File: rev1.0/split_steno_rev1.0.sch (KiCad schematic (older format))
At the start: 82 parts, among them J0 Audio-Jack-4, J1 Audio-Jack-3, K0 KEYSW, K1 KEYSW, K10 KEYSW, K11 KEYSW, K12 KEYSW, K13 KEYSW, K14 KEYSW, K15 KEYSW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

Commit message: added ws2812b
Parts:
- removed J1: Audio-Jack-3, symbol Audio-Jack-3
- removed R16: R, symbol R
- added LED0, LED1, LED2, LED3, LED4: WS2812B, symbol WS2812B
- added Q0: BC547, TO_SOT_Packages_THT:TO-92_Molded_Narrow, symbol BC547
- added R19, R20, R?: R, symbol R
- renumbered R17 to R16, R19 to R17, U1 to U0
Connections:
- net labels added: data0, data1, pwm0, rgb0
- net labels removed: i2c, serial, ws2812b
- wire segments 189 -> 243
- no-connect marks 5 -> 6
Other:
- moved on the sheet: D0, D1, D10, D11, D12, D13, D14, D15, D16, D17, D18, D19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

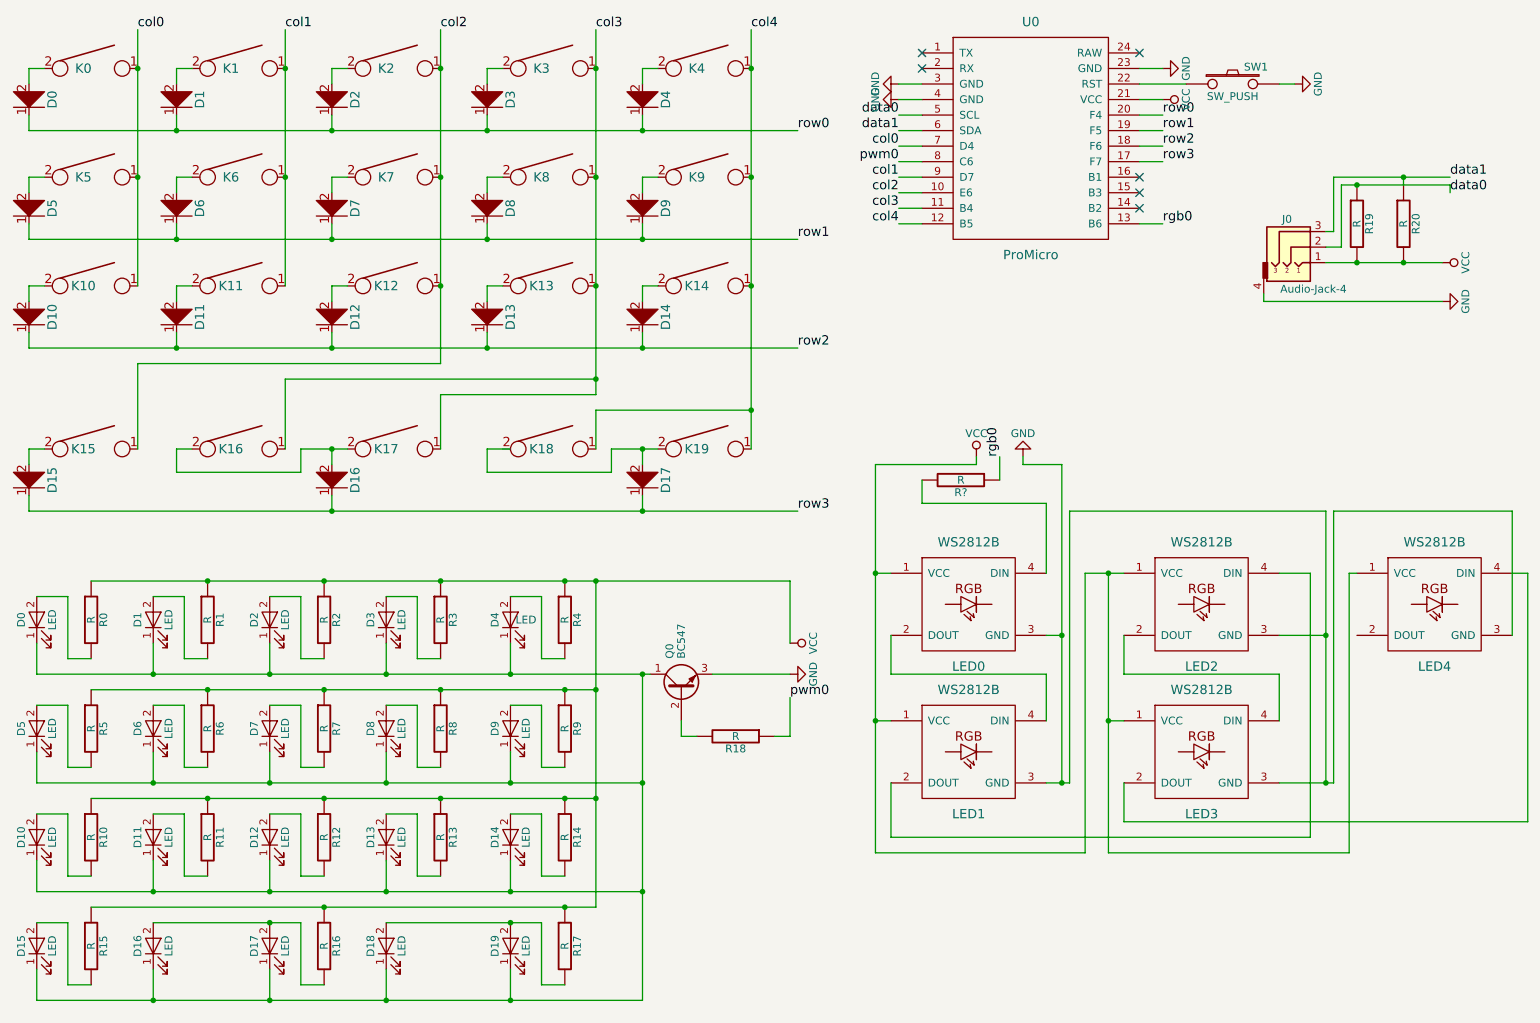
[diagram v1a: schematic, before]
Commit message: cleaned up schematic
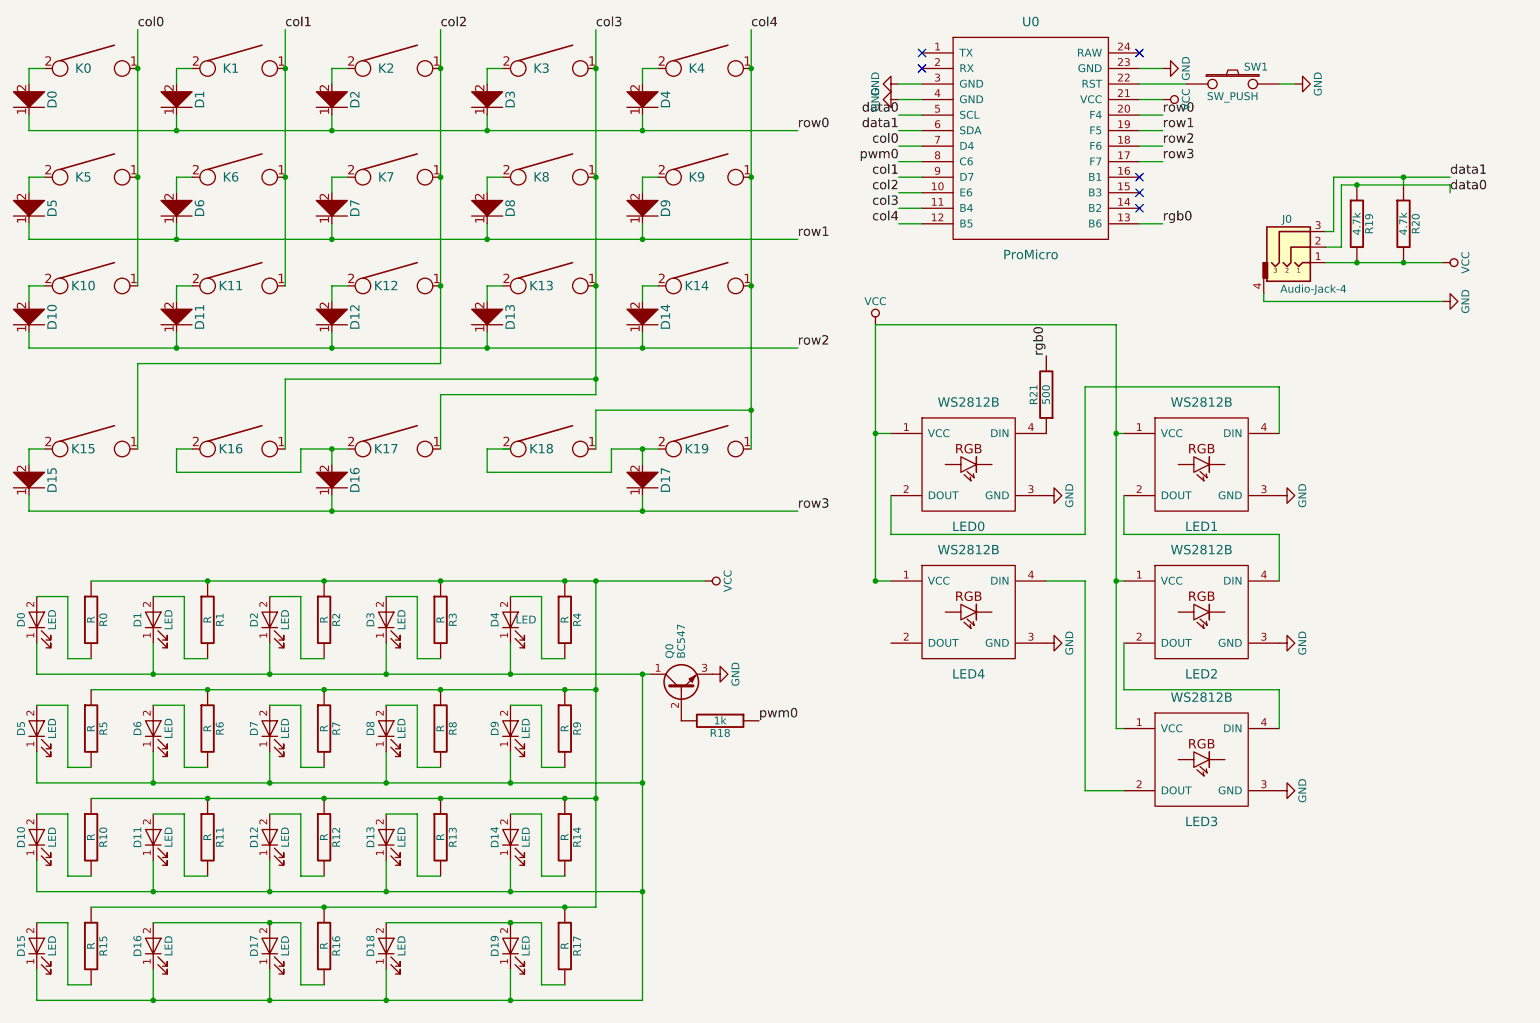
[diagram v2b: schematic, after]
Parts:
- R18: value R -> 1k
- R19, R20: value R -> 4.7k
- R21: renamed from R?; value R -> 500
- renumbered LED2 to LED1, LED3 to LED2, LED4 to LED3, LED1 to LED4
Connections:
- net rgb0: now also R21.2; no longer R21.1
- net at LED0.2 (DOUT): now also LED1.4 (DIN); no longer LED4.4 (DIN)
- net at LED0.4 (DIN): now also R21.1; no longer R21.2
- net at LED4.2 (DOUT): no longer LED1.4 (DIN)
- net at LED3.2 (DOUT): now also LED4.4 (DIN)
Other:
- moved on the sheet: LED0, LED1, LED2, LED3, LED4, R18, R21

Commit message: removed LED backlighting
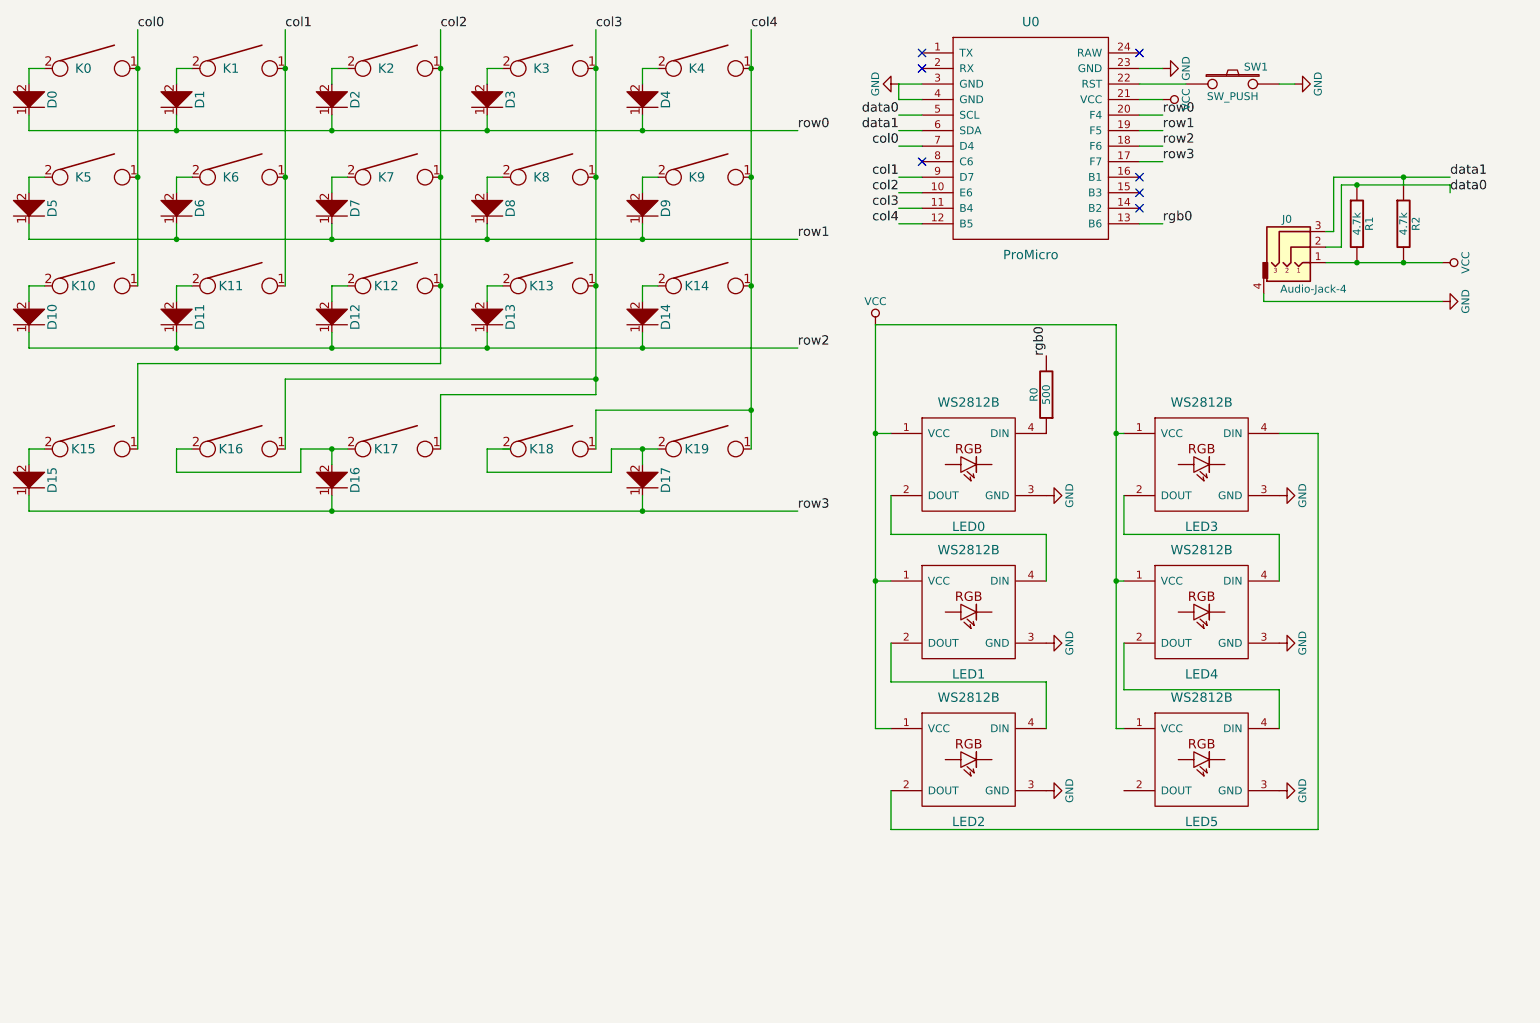
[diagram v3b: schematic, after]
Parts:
- removed D0, D1, D10, D11, D12, D13, D14, D15, D16, D17, D18, D19, D2, D3, D4, D5, D6, D7, D8, D9: LED, symbol LED
- removed Q0: BC547, TO_SOT_Packages_THT:TO-92_Molded_Narrow, symbol BC547
- removed R0, R1, R10, R11, R12, R13, R14, R15, R16, R17, R2, R3, R4, R5, R6, R7, R8, R9: R, symbol R
- removed R18: 1k, symbol R
- added LED2: WS2812B, WS2812B:WS2812B, symbol WS2812B
- D0, D1, D10, D11, D12, D13, D14, D15, D16, D17, D2, D3, D4, D5, D6, D7, D8, D9: footprint (none) -> Keebio-Parts:Diode-dual
- J0: footprint (none) -> Keebio-Parts:TRRS-PJ-320A-dual
- K0, K1, K10, K11, K12, K13, K14, K15, K17, K19, K2, K3, K4, K5, K6, K7, K8, K9: footprint (none) -> Keebio-Parts:Hybrid_PCB_100H_Dual_hole
- K16, K18: footprint (none) -> Keebio-Parts:Hybrid_PCB_200H-dual
- LED0: footprint (none) -> WS2812B:WS2812B
- LED1: renamed from LED4; footprint (none) -> WS2812B:WS2812B
- LED3: renamed from LED1; footprint (none) -> WS2812B:WS2812B
- LED4: renamed from LED2; footprint (none) -> WS2812B:WS2812B
- LED5: renamed from LED3; footprint (none) -> WS2812B:WS2812B
- R0: renamed from R21; footprint (none) -> Keebio-Parts:Resistor-Hybrid
- R1: renamed from R19; footprint (none) -> Keebio-Parts:Resistor-Hybrid
- R2: renamed from R20; footprint (none) -> Keebio-Parts:Resistor-Hybrid
- SW1: footprint (none) -> Keebio-Parts:SW_Tactile_SPST_Angled_MJTP1117
- U0: footprint (none) -> Keebio-Parts:ArduinoProMicro
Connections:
- net GND: now also LED2.3 (GND)
- net VCC: now also LED2.1 (VCC)
- net at LED0.2 (DOUT): now also LED1.4 (DIN); no longer LED3.4 (DIN)
- net at LED1.2 (DOUT): now also LED2.4 (DIN)
- net at LED5.2 (DOUT): no longer LED1.4 (DIN)
- net pwm0: no longer names the net of U0.8 (C6)
- new net: LED2.2 (DOUT), LED3.4 (DIN)
- no-connect marks 6 -> 7

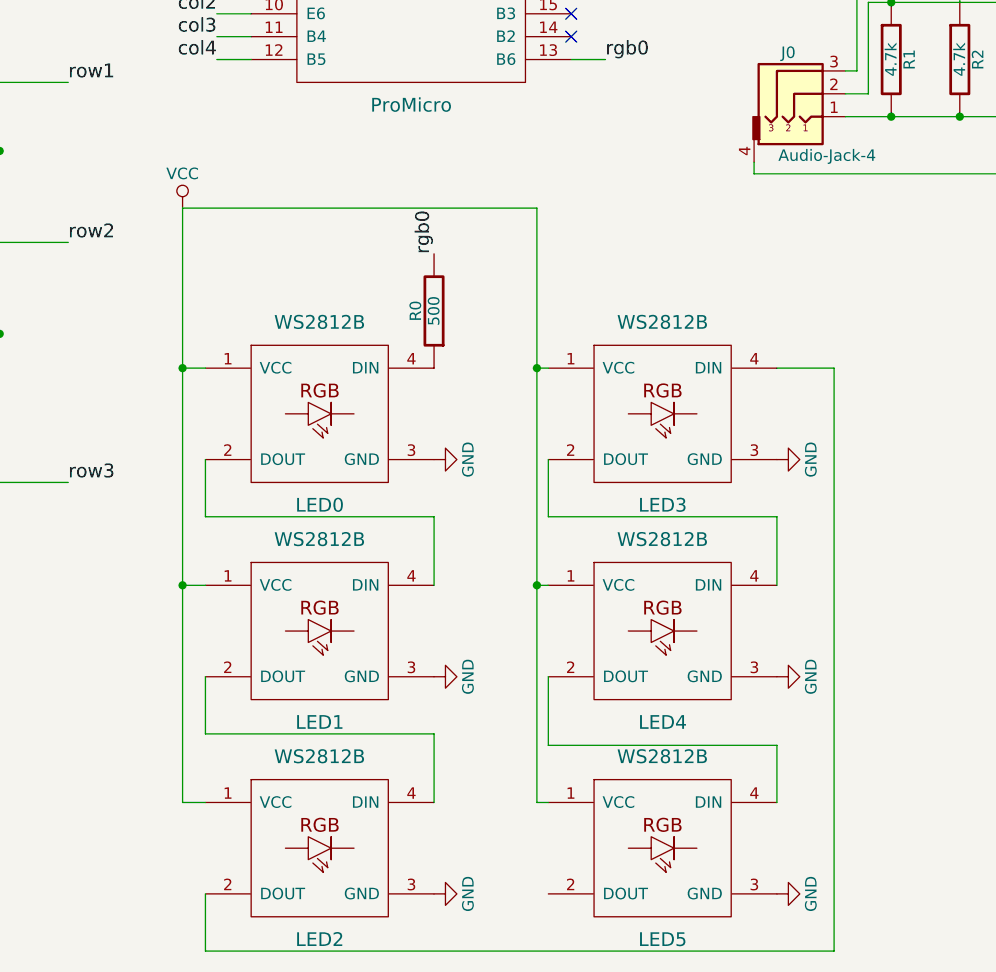
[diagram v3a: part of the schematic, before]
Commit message: removed ws2812b, replaced with breakout
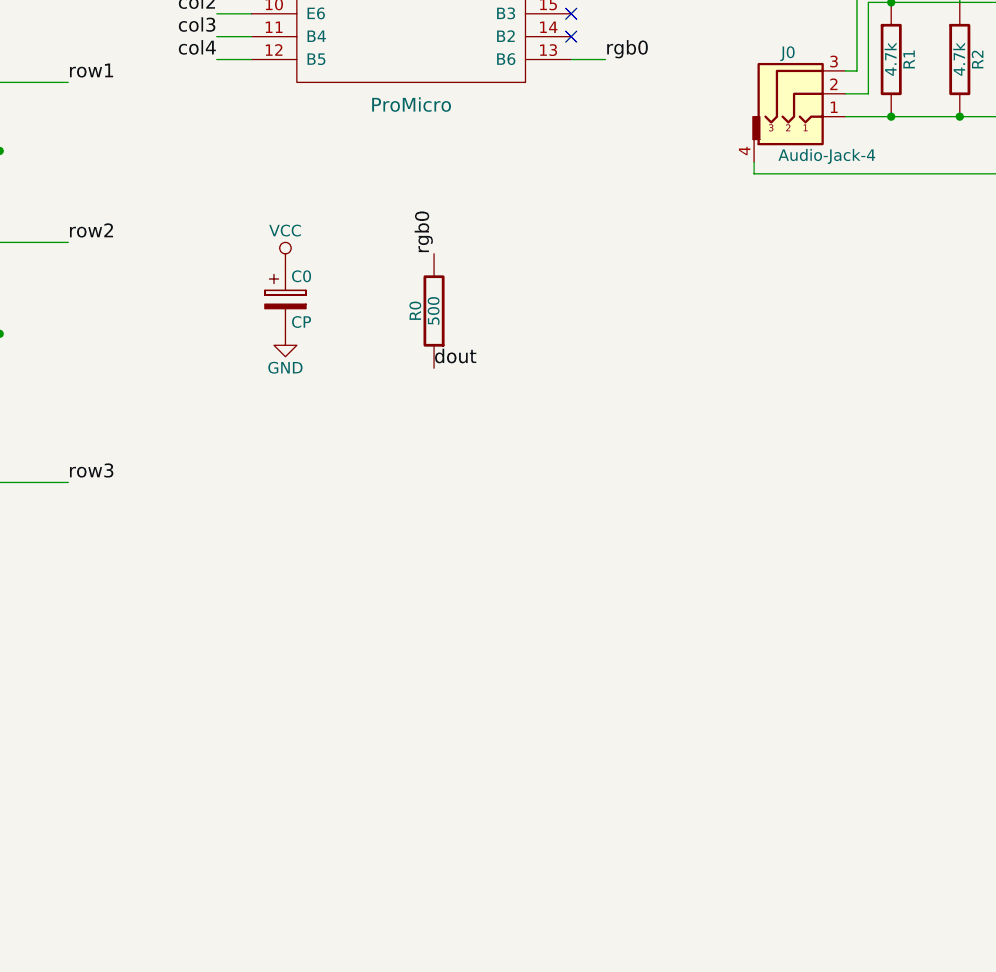
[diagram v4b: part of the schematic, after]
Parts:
- removed LED0, LED1, LED2, LED3, LED4, LED5: WS2812B, WS2812B:WS2812B, symbol WS2812B
- added C0: CP, Capacitors_THT:CP_Radial_D5.0mm_P2.50mm, symbol CP
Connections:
- net GND: now also C0.2
- net VCC: now also C0.1
- net dout: now reaches R0.1
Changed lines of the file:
@@
 Text Label 6900 1550 2    60   ~ 0
 data1
-$Comp
-L WS2812B LED0
-U 1 1 5A986650
-P 7350 3700
-F 0 "LED0" H 7350 3300 60  0000 C CNN
-F 1 "WS2812B" H 7350 4100 60  0000 C CNN
-F 2 "WS2812B:WS2812B" V 7300 3700 60  0001 C CNN
-F 3 "" V 7300 3700 60  0000 C CNN
-	1    7350 3700
-	1    0    0    -1
-$EndComp
-$Comp
-L WS2812B LED1
-U 1 1 5A987126
-P 7350 4650
-F 0 "LED1" H 7350 4250 60  0000 C CNN
-F 1 "WS2812B" H 7350 5050 60  0000 C CNN
-F 2 "WS2812B:WS2812B" V 7300 4650 60  0001 C CNN
-F 3 "" V 7300 4650 60  0000 C CNN
-	1    7350 4650
-	1    0    0    -1
-$EndComp
-$Comp
-L WS2812B LED3
-U 1 1 5A987624
-P 8850 3700
-F 0 "LED3" H 8850 3300 60  0000 C CNN
-F 1 "WS2812B" H 8850 4100 60  0000 C CNN
-F 2 "WS2812B:WS2812B" V 8800 3700 60  0001 C CNN
-F 3 "" V 8800 3700 60  0000 C CNN
-	1    8850 3700
-	1    0    0    -1
-$EndComp
-$Comp
-L WS2812B LED4
-U 1 1 5A98762B
-P 8850 4650
-F 0 "LED4" H 8850 4250 60  0000 C CNN
-F 1 "WS2812B" H 8850 5050 60  0000 C CNN
-F 2 "WS2812B:WS2812B" V 8800 4650 60  0001 C CNN
-F 3 "" V 8800 4650 60  0000 C CNN
-	1    8850 4650
-	1    0    0    -1
-$EndComp
-$Comp
-L VCC #PWR07
-U 1 1 5A98C079
-P 6750 2800
-F 0 "#PWR07" H 6750 2650 50  0001 C CNN
-F 1 "VCC" H 6750 2950 50  0000 C CNN
-F 2 "" H 6750 2800 50  0001 C CNN
-F 3 "" H 6750 2800 50  0001 C CNN
-	1    6750 2800
-	1    0    0    -1
-$EndComp
-$Comp
-L GND #PWR08
-U 1 1 5A98C29D
-P 9350 3900
-F 0 "#PWR08" H 9350 3650 50  0001 C CNN
-F 1 "GND" H 9350 3750 50  0000 C CNN
-F 2 "" H 9350 3900 50  0001 C CNN
-F 3 "" H 9350 3900 50  0001 C CNN
-	1    9350 3900
-	0    -1   -1   0
-$EndComp
 Text Label 7850 3000 1    60   ~ 0
 rgb0
@@
 Text Label 8600 2150 0    60   ~ 0
 rgb0
-$Comp
-L GND #PWR09
-U 1 1 5A9901E0
-P 7850 3900
-F 0 "#PWR09" H 7850 3650 50  0001 C CNN
-F 1 "GND" H 7850 3750 50  0000 C CNN
-F 2 "" H 7850 3900 50  0001 C CNN
-F 3 "" H 7850 3900 50  0001 C CNN
-	1    7850 3900
-	0    -1   -1   0
-$EndComp
-$Comp
-L GND #PWR010
-U 1 1 5A9903AB
-P 7850 4850
-F 0 "#PWR010" H 7850 4600 50  0001 C CNN
-F 1 "GND" H 7850 4700 50  0000 C CNN
-F 2 "" H 7850 4850 50  0001 C CNN
-F 3 "" H 7850 4850 50  0001 C CNN
-	1    7850 4850
-	0    -1   -1   0
-$EndComp
-$Comp
-L GND #PWR011
-U 1 1 5A990689
-P 9350 4850
-F 0 "#PWR011" H 9350 4600 50  0001 C CNN
-F 1 "GND" H 9350 4700 50  0000 C CNN
-F 2 "" H 9350 4850 50  0001 C CNN
-F 3 "" H 9350 4850 50  0001 C CNN
-	1    9350 4850
-	0    -1   -1   0
-$EndComp
-$Comp
-L GND #PWR012
-U 1 1 5A9907FB
-P 9350 5800
-F 0 "#PWR012" H 9350 5550 50  0001 C CNN
-F 1 "GND" H 9350 5650 50  0000 C CNN
-F 2 "" H 9350 5800 50  0001 C CNN
-F 3 "" H 9350 5800 50  0001 C CNN
-	1    9350 5800
-	0    -1   -1   0
-$EndComp
-$Comp
-L WS2812B LED5
-U 1 1 5A987719
-P 8850 5600
-F 0 "LED5" H 8850 5200 60  0000 C CNN
-F 1 "WS2812B" H 8850 6000 60  0000 C CNN
-F 2 "WS2812B:WS2812B" V 8800 5600 60  0001 C CNN
-F 3 "" V 8800 5600 60  0000 C CNN
-	1    8850 5600
-	1    0    0    -1
-$EndComp
 Wire Wire Line
 	9350 1250 9450 1250
@@
 	6900 1550 7050 1550
 Wire Wire Line
-	6850 3500 6750 3500
-Wire Wire Line
-	6750 4450 6850 4450
-Connection ~ 6750 3500
-Wire Wire Line
 	8450 2150 8600 2150
-Connection ~ 6750 4450
-Wire Wire Line
-	6750 2800 6750 5400
-Wire Wire Line
-	6750 2800 8300 2800
-Wire Wire Line
-	8300 2800 8300 5400
-Wire Wire Line
-	8300 3500 8350 3500
-Wire Wire Line
-	8300 4450 8350 4450
-Connection ~ 8300 3500
-Wire Wire Line
-	8300 5400 8350 5400
-Connection ~ 8300 4450
-Wire Wire Line
-	8350 3900 8350 4150
-Wire Wire Line
-	8350 4150 9350 4150
-Wire Wire Line
-	9350 4150 9350 4450
-Wire Wire Line
-	8350 4850 8350 5150
-Wire Wire Line
-	8350 5150 9350 5150
-Wire Wire Line
-	9350 5150 9350 5400
-Wire Wire Line
-	6850 3900 6850 4150
+NoConn ~ 7050 1750
+Wire Wire Line
+	6900 1350 6900 1250
 $Comp
-L WS2812B LED2
-U 1 1 5A9F4BAC
-P 7350 5600
-F 0 "LED2" H 7350 5200 60  0000 C CNN
-F 1 "WS2812B" H 7350 6000 60  0000 C CNN
-F 2 "WS2812B:WS2812B" V 7300 5600 60  0001 C CNN
-F 3 "" V 7300 5600 60  0000 C CNN
-	1    7350 5600
+L CP C0
+U 1 1 5AA06AA7
+P 7200 3200
+F 0 "C0" H 7225 3300 50  0000 L CNN
+F 1 "CP" H 7225 3100 50  0000 L CNN
+F 2 "Capacitors_THT:CP_Radial_D5.0mm_P2.50mm" H 7238 3050 50  0001 C CNN
+F 3 "" H 7200 3200 50  0001 C CNN
+	1    7200 3200
 	1    0    0    -1
 $EndComp
-Wire Wire Line
-	6850 4150 7850 4150
-Wire Wire Line
-	7850 4150 7850 4450
-Wire Wire Line
-	6850 4850 6850 5100
-Wire Wire Line
-	6850 5100 7850 5100
-Wire Wire Line
-	7850 5100 7850 5400
-Wire Wire Line
-	6750 5400 6850 5400
-Wire Wire Line
-	6850 5800 6850 6050
-Wire Wire Line
-	6850 6050 9600 6050
-Wire Wire Line
-	9600 6050 9600 3500
-Wire Wire Line
-	9600 3500 9350 3500
 $Comp
-L GND #PWR013
-U 1 1 5A9F55D9
-P 7850 5800
-F 0 "#PWR013" H 7850 5550 50  0001 C CNN
-F 1 "GND" H 7850 5650 50  0000 C CNN
-F 2 "" H 7850 5800 50  0001 C CNN
-F 3 "" H 7850 5800 50  0001 C CNN
-	1    7850 5800
-	0    -1   -1   0
+L VCC #PWR07
+U 1 1 5AA06BB0
+P 7200 3050
+F 0 "#PWR07" H 7200 2900 50  0001 C CNN
+F 1 "VCC" H 7200 3200 50  0000 C CNN
+F 2 "" H 7200 3050 50  0001 C CNN
+F 3 "" H 7200 3050 50  0001 C CNN
+	1    7200 3050
+	1    0    0    -1
 $EndComp
-NoConn ~ 7050 1750
-Wire Wire Line
-	6900 1350 6900 1250
+$Comp
+L GND #PWR08
+U 1 1 5AA06C4D
+P 7200 3350
+F 0 "#PWR08" H 7200 3100 50  0001 C CNN
+F 1 "GND" H 7200 3200 50  0000 C CNN
+F 2 "" H 7200 3350 50  0001 C CNN
+F 3 "" H 7200 3350 50  0001 C CNN
+	1    7200 3350
+	1    0    0    -1
+$EndComp
+Text Label 7850 3500 0    60   ~ 0
+dout
 $EndSCHEMATC
